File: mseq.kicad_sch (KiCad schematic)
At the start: 64 parts, among them J1 Conn_01x04_Pin, J2 TC2030-NL, P1 USB_C_Plug_USB2.0, SW1 SW_SPST, SW2 BOOT, SW3 RESET, SW4 SW_SPST, U2 SN74AHCT125DR, U3 MCP1703Ax-330xxTT, U4 CP2102N-Axx-xQFN20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

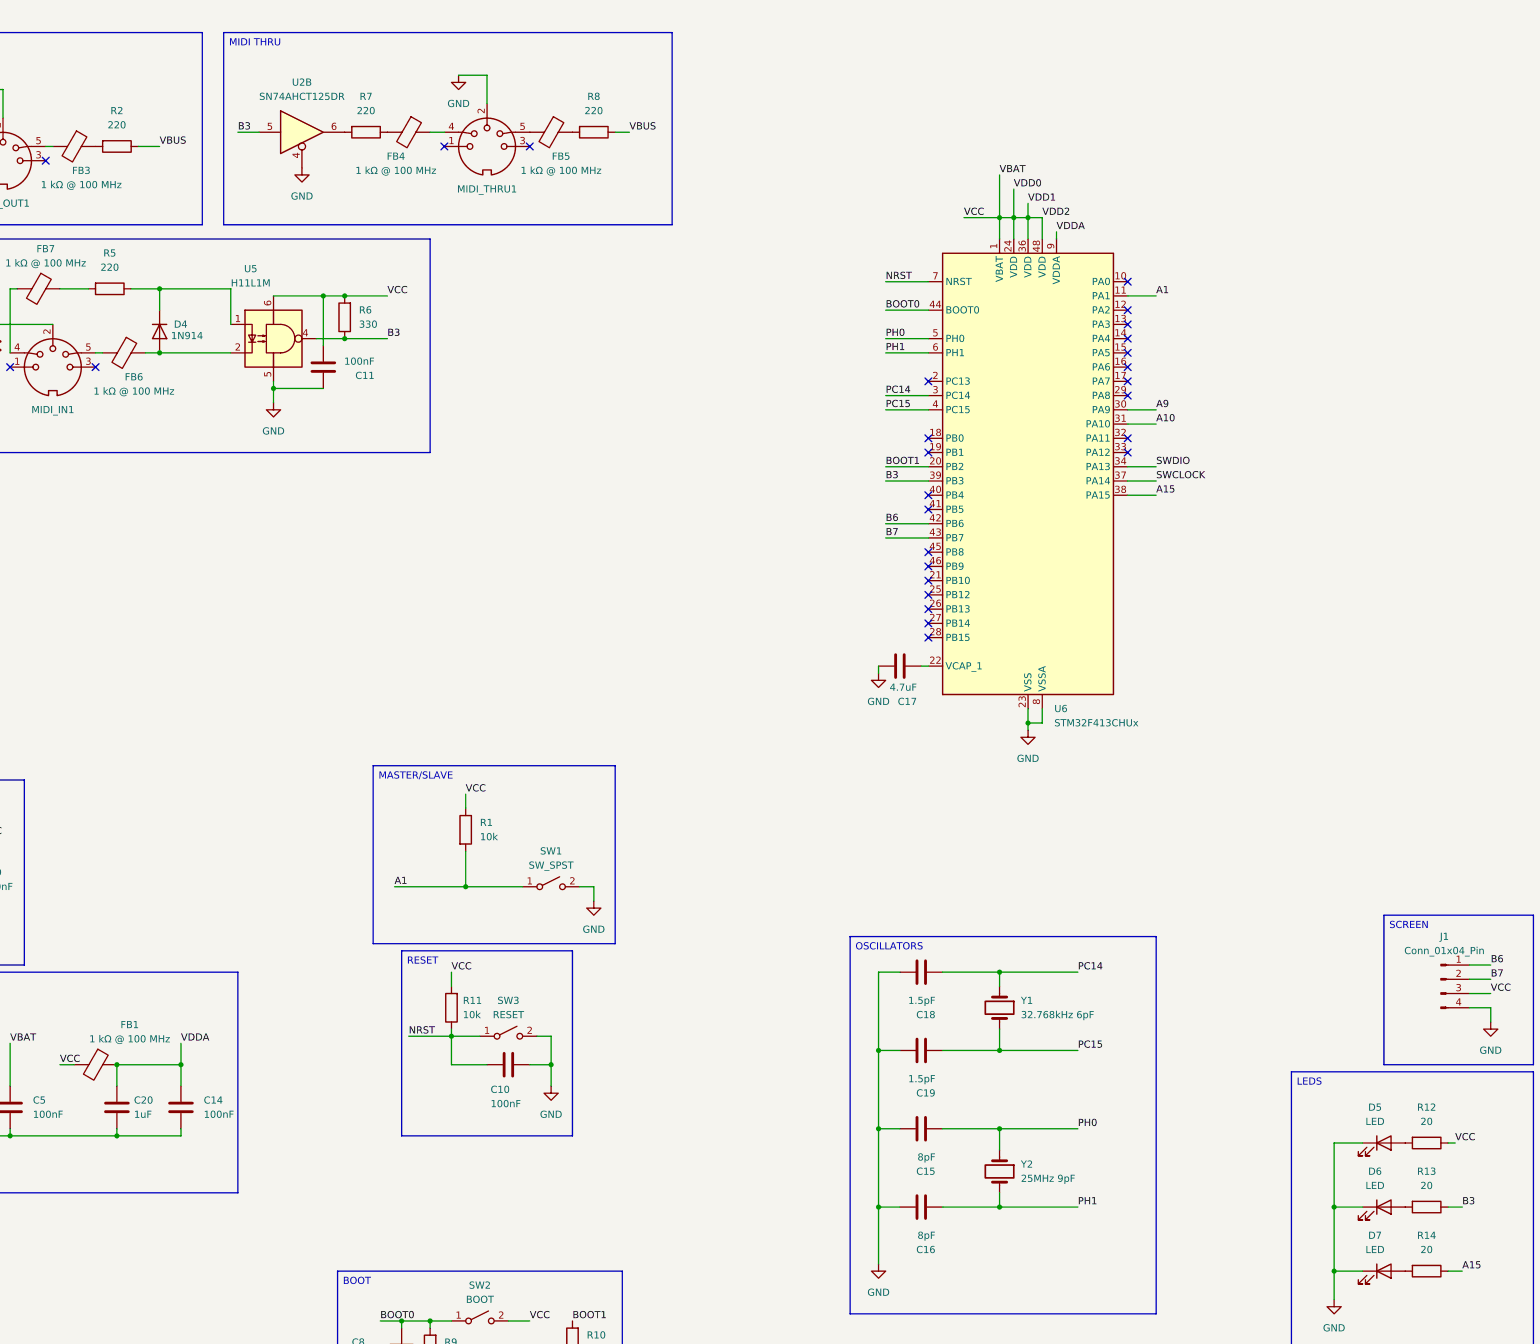
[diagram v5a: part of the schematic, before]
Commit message: Resistor for MIDI done
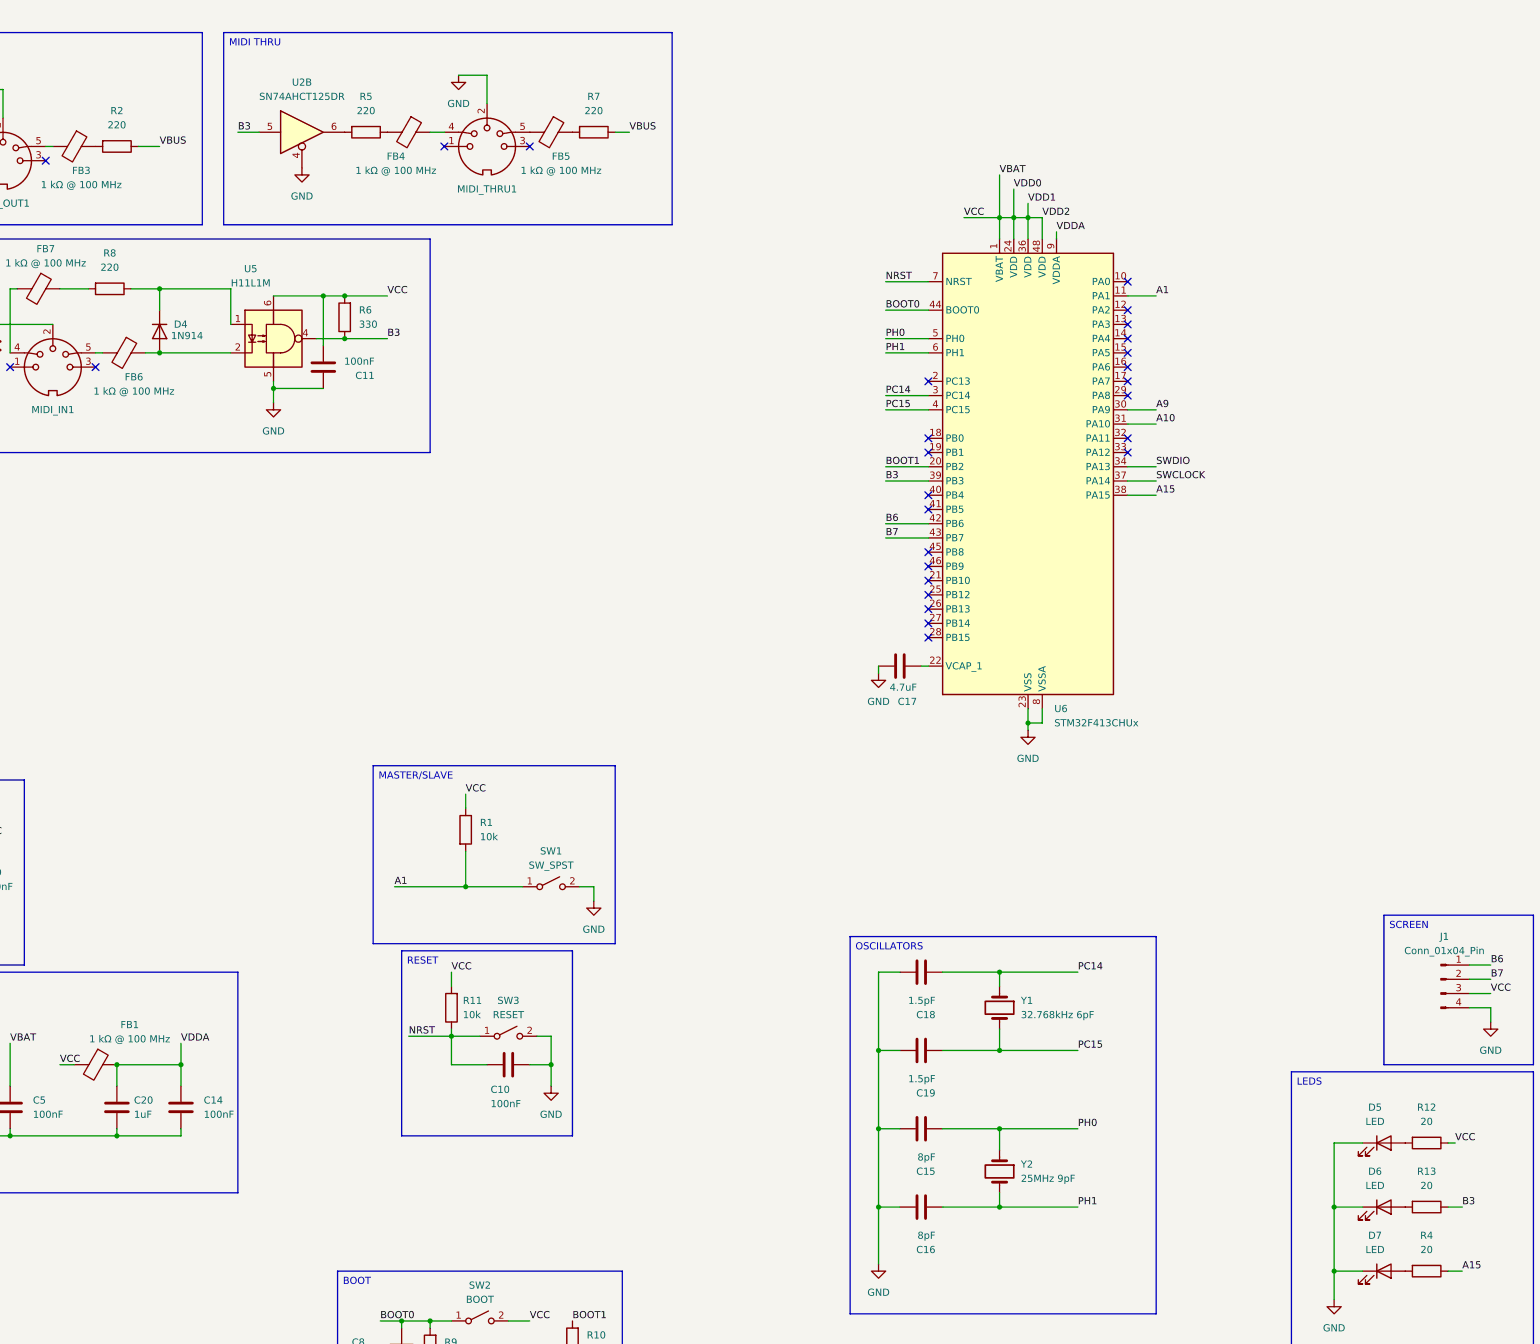
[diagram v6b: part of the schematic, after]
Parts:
- removed R14: 20, Resistor_SMD:R_0201_0603Metric, symbol Device:R
- added R4: 20, Resistor_SMD:R_0201_0603Metric, symbol Device:R
- R2, R3, R5, R7, R8: footprint Resistor_SMD:R_0201_0603Metric -> Resistor_SMD:R_0603_1608Metric; MPN (none) -> CRCW0603220RJNEA
- R6: footprint Resistor_SMD:R_0201_0603Metric -> Resistor_SMD:R_0603_1608Metric; MPN (none) -> CRCW0603330RJNEA
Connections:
- net A15: now also R4.1
- net VBUS: now also R7.1; no longer R8.1
- net at D4.1 (K), U5.1: now also R8.1; no longer R5.1
- net at FB7.1: now also R8.2; no longer R5.2
- net at U2.6: now also R5.2; no longer R7.2
- net at D7.2 (A): now also R4.2
- net at FB5.1: now also R7.2; no longer R8.2
- net at FB4.2: now also R5.1; no longer R7.1

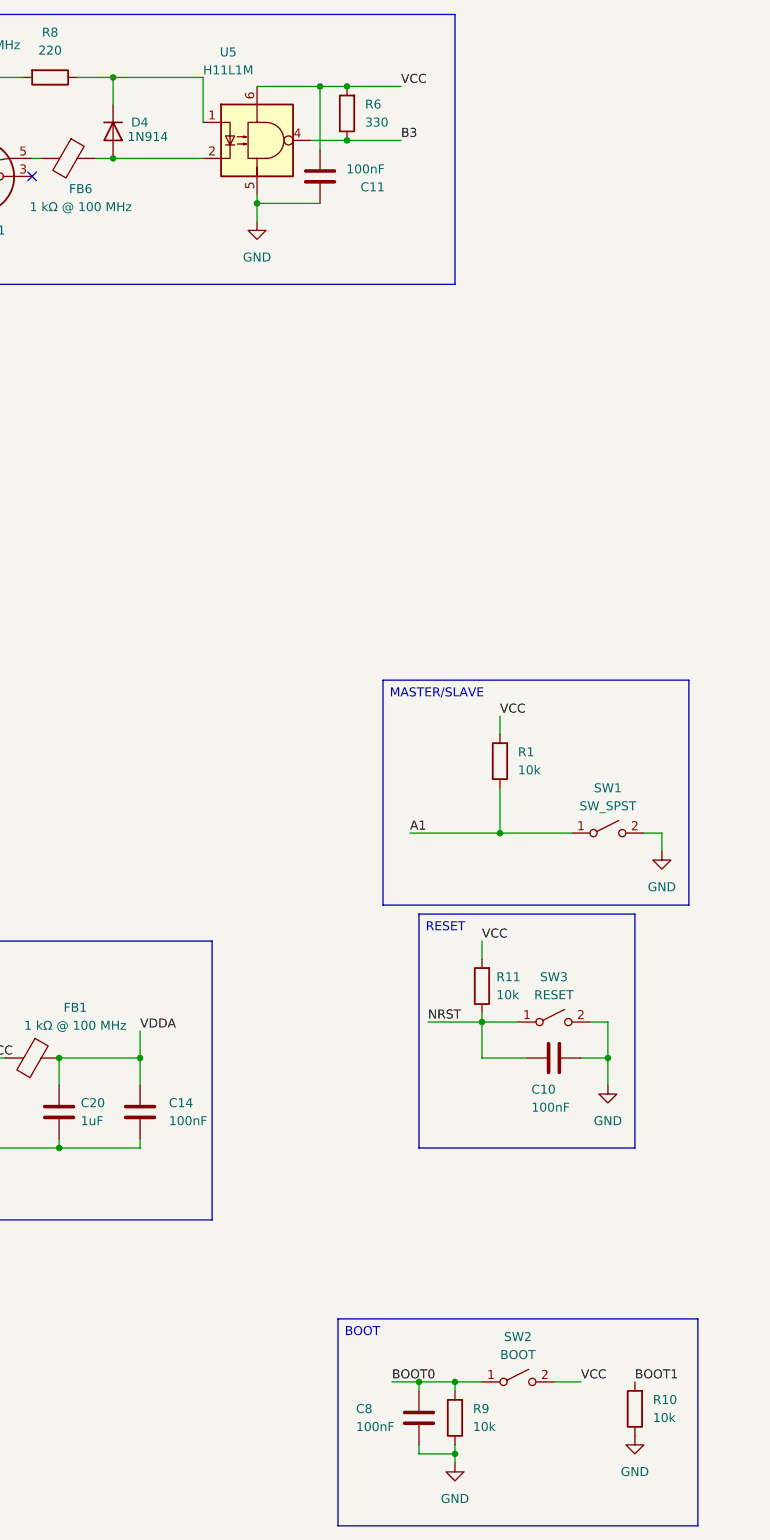
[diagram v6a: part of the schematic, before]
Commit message: MPN for resistors and diodes added
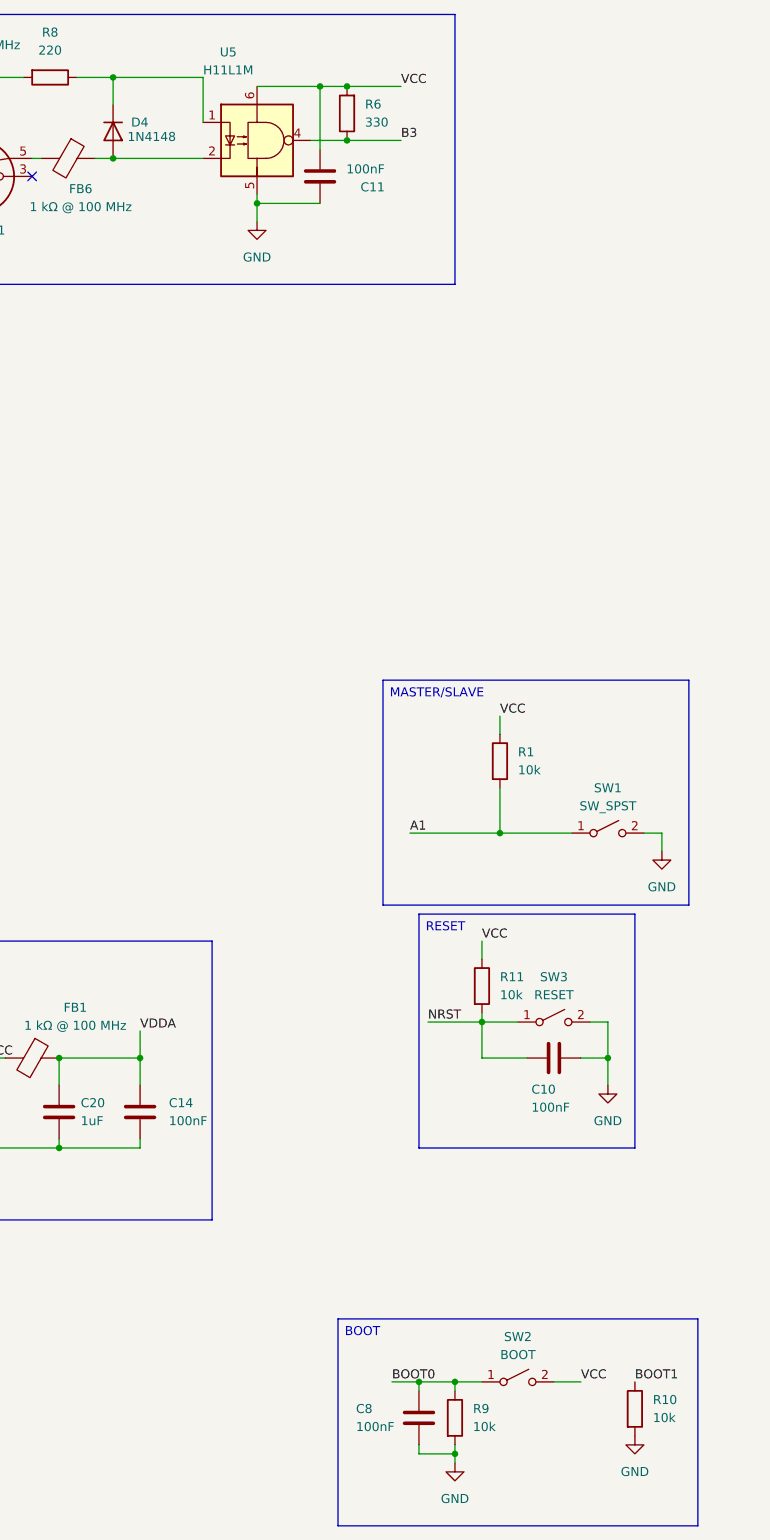
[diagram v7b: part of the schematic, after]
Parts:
- D4: value 1N914 -> 1N4148; footprint Diode_SMD:D_0201_0603Metric -> Diode_SMD:D_SOD-123; MPN (none) -> 1N4148W-E3-08
- R1, R10, R11, R9: footprint Resistor_SMD:R_0201_0603Metric -> Resistor_SMD:R_0603_1608Metric; MPN (none) -> CRGCQ0603J10K
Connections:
- net BOOT0: now also R9.1; no longer R9.2
- net BOOT1: now also R10.1; no longer R10.2
- net GND: now also R10.2, R9.2; no longer R10.1, R9.1
- net NRST: now also R11.2; no longer R11.1
- net VBAT: now also R11.1; no longer R11.2
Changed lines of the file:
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@@
 	(symbol
 		(lib_id "Device:R")
-		(at 166.37 250.19 180)
+		(at 140.97 251.46 0)
 		(unit 1)
 		(exclude_from_sim no)
@@
 		(dnp no)
 		(fields_autoplaced yes)
-		(property "Reference" "R10"
-			(at 168.91 248.9199 0)
+		(property "Reference" "R9"
+			(at 143.51 250.1899 0)
 			(effects
 				(font
 					(size 1.27 1.27)
 				)
-				(justify right)
+				(justify left)
 			)
 		)
 		(property "Value" "10k"
-			(at 168.91 251.4599 0)
+			(at 143.51 252.7299 0)
 			(effects
 				(font
 					(size 1.27 1.27)
 				)
-				(justify right)
+				(justify left)
 			)
 		)
-		(property "Footprint" "Resistor_SMD:R_0201_0603Metric"
-			(at 168.148 250.19 90)
+		(property "Footprint" "Resistor_SMD:R_0603_1608Metric"
+			(at 139.192 251.46 90)
 			(effects
 				(font
@@
 		)
 		(property "Datasheet" "~"
-			(at 166.37 250.19 0)
+			(at 140.97 251.46 0)
 			(effects
 				(font
@@
 		)
 		(property "Description" "Resistor"
-			(at 166.37 250.19 0)
+			(at 140.97 251.46 0)
+			(effects
+				(font
+					(size 1.27 1.27)
+				)
+				(hide yes)
+			)
+		)
+		(property "MPN" "CRGCQ0603J10K"
+			(at 140.97 251.46 0)
 			(effects
 				(font
@@
 			(project "mseq"
 				(path "/4f5593bf-962d-4fa9-909b-449bd6b94d0f"
-					(reference "R10")
+					(reference "R9")
 					(unit 1)
 				)
@@
 	)
 	(symbol
+		(lib_id "Device:R")
+		(at 144.78 190.5 0)
+		(unit 1)
+		(exclude_from_sim no)
+		(in_bom yes)
+		(on_board yes)
+		(dnp no)
+		(fields_autoplaced yes)
+		(property "Reference" "R11"
+			(at 147.32 189.2299 0)
+			(effects
+				(font
+					(size 1.27 1.27)
+				)
+				(justify left)
+			)
+		)
+		(property "Value" "10k"
+			(at 147.32 191.7699 0)
+			(effects
+				(font
+					(size 1.27 1.27)
+				)
+				(justify left)
+			)
+		)
+		(property "Footprint" "Resistor_SMD:R_0603_1608Metric"
+			(at 143.002 190.5 90)
+			(effects
+				(font
+					(size 1.27 1.27)
+				)
+				(hide yes)
+			)
+		)
+		(property "Datasheet" "~"
+			(at 144.78 190.5 0)
+			(effects
+				(font
+					(size 1.27 1.27)
+				)
+				(hide yes)
+			)
+		)
+		(property "Description" "Resistor"
+			(at 144.78 190.5 0)
+			(effects
+				(font
+					(size 1.27 1.27)
+				)
+				(hide yes)
+			)
+		)
+		(property "MPN" "CRGCQ0603J10K"
+			(at 144.78 190.5 0)
+			(effects
+				(font
+					(size 1.27 1.27)
+				)
+				(hide yes)
+			)
+		)
+		(pin "1"
+		)
+		(pin "2"
+		)
+		(instances
+			(project "mseq"
+				(path "/4f5593bf-962d-4fa9-909b-449bd6b94d0f"
+					(reference "R11")
+					(unit 1)
+				)
+			)
+		)
+	)
+	(symbol
 		(lib_id "Power_Protection:SP0503BAHT")
 		(at 384.81 231.14 0)
@@
 			)
 		)
-		(property "Footprint" "Resistor_SMD:R_0201_0603Metric"
+		(property "Footprint" "Resistor_SMD:R_0603_1608Metric"
 			(at 145.542 158.75 90)
 			(effects
@@
 			)
 		)
+		(property "MPN" "CRGCQ0603J10K"
+			(at 147.32 158.75 0)
+			(effects
+				(font
+					(size 1.27 1.27)
+				)
+				(hide yes)
+			)
+		)
 		(pin "1"
 		)
@@
 			)
 		)
-		(property "Value" "1N914"
+		(property "Value" "1N4148"
 			(at 94.742 70.612 90)
 			(effects
@@
 			)
 		)
-		(property "Footprint" "Diode_SMD:D_0201_0603Metric"
+		(property "Footprint" "Diode_SMD:D_SOD-123"
 			(at 88.265 69.85 0)
 			(effects
@@
 			)
 		)
-		(property "Datasheet" "http://www.vishay.com/docs/85622/1n914.pdf"
-			(at 92.71 69.85 0)
-			(effects
-				(font
-					(size 1.27 1.27)
-				)
-				(hide yes)
-			)
-		)
-		(property "Description" "100V 0.3A Small Signal Fast Switching Diode, DO-35"
+		(property "Datasheet" ""
 			(at 92.71 69.85 0)
 			(effects
@@
 			)
 		)
-		(property "Sim.Device" "D"
+		(property "Description" ""
 			(at 92.71 69.85 0)
 			(effects
@@
 			)
 		)
-		(property "Sim.Pins" "1=K 2=A"
-			(at 92.71 69.85 0)
+		(property "MPN" "1N4148W-E3-08"
+			(at 92.71 69.85 90)
 			(effects
 				(font
@@
 	)
 	(symbol
+		(lib_id "Device:R")
+		(at 166.37 250.19 0)
+		(unit 1)
+		(exclude_from_sim no)
+		(in_bom yes)
+		(on_board yes)
+		(dnp no)
+		(fields_autoplaced yes)
+		(property "Reference" "R10"
+			(at 168.91 248.9199 0)
+			(effects
+				(font
+					(size 1.27 1.27)
+				)
+				(justify left)
+			)
+		)
+		(property "Value" "10k"
+			(at 168.91 251.4599 0)
+			(effects
+				(font
+					(size 1.27 1.27)
+				)
+				(justify left)
+			)
+		)
+		(property "Footprint" "Resistor_SMD:R_0603_1608Metric"
+			(at 164.592 250.19 90)
+			(effects
+				(font
+					(size 1.27 1.27)
+				)
+				(hide yes)
+			)
+		)
+		(property "Datasheet" "~"
+			(at 166.37 250.19 0)
+			(effects
+				(font
+					(size 1.27 1.27)
+				)
+				(hide yes)
+			)
+		)
+		(property "Description" "Resistor"
+			(at 166.37 250.19 0)
+			(effects
+				(font
+					(size 1.27 1.27)
+				)
+				(hide yes)
+			)
+		)
+		(property "MPN" "CRGCQ0603J10K"
+			(at 166.37 250.19 0)
+			(effects
+				(font
+					(size 1.27 1.27)
+				)
+				(hide yes)
+			)
+		)
+		(pin "1"
+		)
+		(pin "2"
+		)
+		(instances
+			(project "mseq"
+				(path "/4f5593bf-962d-4fa9-909b-449bd6b94d0f"
+					(reference "R10")
+					(unit 1)
+				)
+			)
+		)
+	)
+	(symbol
 		(lib_id "Device:C")
 		(at 17.78 208.28 0)
@@
 	)
 	(symbol
-		(lib_id "Device:R")
-		(at 144.78 190.5 180)
-		(unit 1)
-		(exclude_from_sim no)
-		(in_bom yes)
-		(on_board yes)
-		(dnp no)
-		(property "Reference" "R11"
-			(at 146.812 189.23 0)
-			(effects
-				(font
-					(size 1.27 1.27)
-				)
-				(justify right)
-			)
-		)
-		(property "Value" "10k"
-			(at 146.812 191.77 0)
-			(effects
-				(font
-					(size 1.27 1.27)
-				)
-				(justify right)
-			)
-		)
-		(property "Footprint" "Resistor_SMD:R_0201_0603Metric"
-			(at 146.558 190.5 90)
-			(effects
-				(font
-					(size 1.27 1.27)
-				)
-				(hide yes)
-			)
-		)
-		(property "Datasheet" "~"
-			(at 144.78 190.5 0)
-			(effects
-				(font
-					(size 1.27 1.27)
-				)
-				(hide yes)
-			)
-		)
-		(property "Description" "Resistor"
-			(at 144.78 190.5 0)
-			(effects
-				(font
-					(size 1.27 1.27)
-				)
-				(hide yes)
-			)
-		)
-		(pin "1"
-		)
-		(pin "2"
-		)
-		(instances
-			(project "mseq"
-				(path "/4f5593bf-962d-4fa9-909b-449bd6b94d0f"
-					(reference "R11")
-					(unit 1)
-				)
-			)
-		)
-	)
-	(symbol
 		(lib_id "Device:C")
 		(at 66.04 208.28 0)
@@
 					(unit 1)
 				)
-			)
-		)
-	)
-	(symbol
-		(lib_id "Device:R")
-		(at 140.97 251.46 180)
-		(unit 1)
-		(exclude_from_sim no)
-		(in_bom yes)
-		(on_board yes)
-		(dnp no)
-		(fields_autoplaced yes)
-		(property "Reference" "R9"
-			(at 143.51 250.1899 0)
-			(effects
-				(font
-					(size 1.27 1.27)
-				)
-				(justify right)
-			)
-		)
-		(property "Value" "10k"
-			(at 143.51 252.7299 0)
-			(effects
-				(font
-					(size 1.27 1.27)
-				)
-				(justify right)
-			)
-		)
-		(property "Footprint" "Resistor_SMD:R_0201_0603Metric"
-			(at 142.748 251.46 90)
-			(effects
-				(font
-					(size 1.27 1.27)
-				)
-				(hide yes)
-			)
-		)
-		(property "Datasheet" "~"
-			(at 140.97 251.46 0)
-			(effects
-				(font
-					(size 1.27 1.27)
-				)
-				(hide yes)
-			)
-		)
-		(property "Description" "Resistor"
-			(at 140.97 251.46 0)
-			(effects
-				(font
-					(size 1.27 1.27)
-				)
-				(hide yes)
-			)
-		)
-		(pin "1"
-		)
-		(pin "2"
-		)
-		(instances
-			(project "mseq"
-				(path "/4f5593bf-962d-4fa9-909b-449bd6b94d0f"
-					(reference "R9")
-					(unit 1)
-				)
